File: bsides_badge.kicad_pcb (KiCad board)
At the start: 2 copper layers, 100.5 x 100.5 mm, 2 parts

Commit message: V2 badge
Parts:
- removed the REF** at (125.0, 60.0)
- removed the REF** at (175.0, 60.0)
- added BT1: Battery_Cell, badge:CoinCell_no_silk, F.Cu at (99.7, 83.8)
- added D1: LED, LEDs:LED_0805, F.Cu at (165.7, 53.3)
- added G***: LOGO, graphics:bsides, F.Cu at (135.6, 68.5)
- added J1: Conn_01x16, Pin_Headers:Pin_Header_Straight_1x16_Pitch2.54mm, F.Cu at (106.7, 55.9)
- added J2: Conn_01x01, Pin_Headers:Pin_Header_Straight_1x01_Pitch2.54mm, F.Cu at (111.8, 55.9)
- added R1: 56R, Resistors_SMD:R_0805_HandSoldering, F.Cu at (153.0, 53.3)
- added REF**: keychain_hole, badge:keychain_hole, F.Cu at (96.5, 73.7)
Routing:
- net Net-(J1-Pad1): track 0.00 -> 120.4 mm
- net Net-(BT1-Pad2): track 0.00 -> 81.6 mm
- net Net-(BT1-Pad1): track 0.00 -> 79.5 mm
- net Net-(D1-Pad2): track 0.00 -> 10.2 mm
- added copper zone on F.Cu, net (none)
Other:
- board size 100.5 x 100.5 mm -> 88.9 x 50.8 mm
- net class Default: clearance 0.2 -> 0.4; trace_width 0.25 -> 0.5
- rule trace_clearance: 0.2 -> 0.4

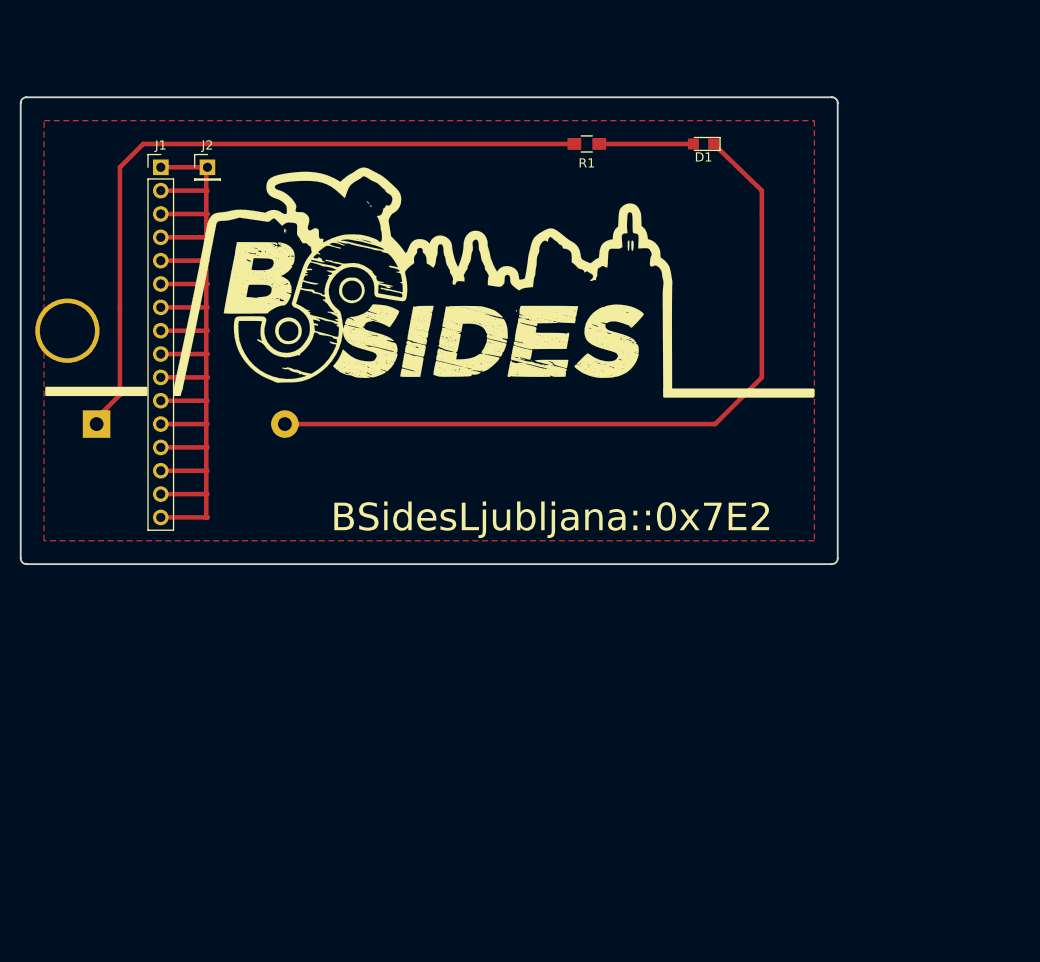
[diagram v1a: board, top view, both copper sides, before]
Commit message: Change to credit card format and rebalanced battery
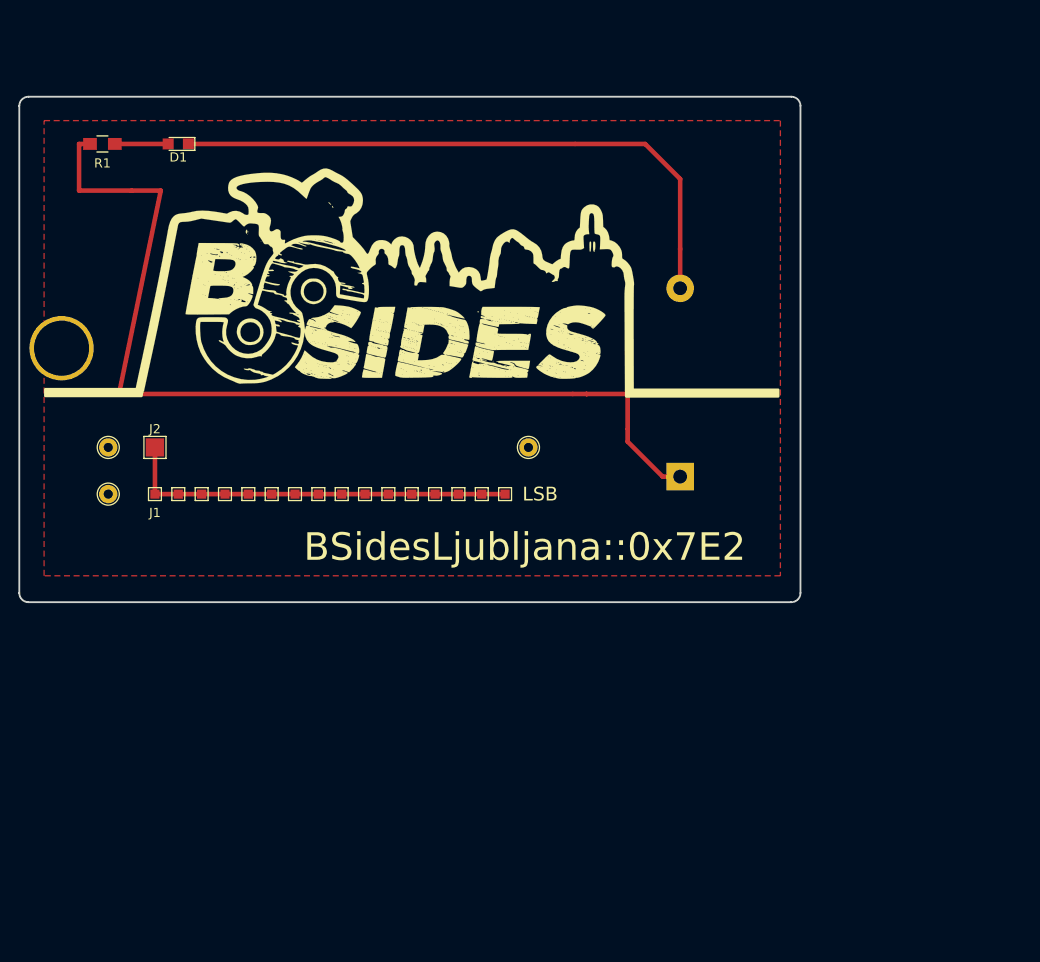
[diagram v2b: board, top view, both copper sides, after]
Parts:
- removed the J1 at (106.7, 55.9)
- added J1: Conn_01x16, TestPoint:TestPoint_Pad_1.0x1.0mm, F.Cu at (144.1, 91.4)
- added J1: Conn_01x16, TestPoint:TestPoint_Pad_1.0x1.0mm, F.Cu at (121.3, 91.4)
- added J1: Conn_01x16, TestPoint:TestPoint_Pad_1.0x1.0mm, F.Cu at (118.7, 91.4)
- added J1: Conn_01x16, TestPoint:TestPoint_Pad_1.0x1.0mm, F.Cu at (116.2, 91.4)
- added J1: Conn_01x16, TestPoint:TestPoint_Pad_1.0x1.0mm, F.Cu at (113.7, 91.4)
- added J1: Conn_01x16, TestPoint:TestPoint_Pad_1.0x1.0mm, F.Cu at (111.1, 91.4)
- added J1: Conn_01x16, TestPoint:TestPoint_Pad_1.0x1.0mm, F.Cu at (108.6, 91.4)
- added J1: Conn_01x16, TestPoint:TestPoint_Pad_1.0x1.0mm, F.Cu at (106.0, 91.4)
- added J1: Conn_01x16, TestPoint:TestPoint_Pad_1.0x1.0mm, F.Cu at (141.6, 91.4)
- added J1: Conn_01x16, TestPoint:TestPoint_Pad_1.0x1.0mm, F.Cu at (139.1, 91.4)
- added J1: Conn_01x16, TestPoint:TestPoint_Pad_1.0x1.0mm, F.Cu at (136.5, 91.4)
- added J1: Conn_01x16, TestPoint:TestPoint_Pad_1.0x1.0mm, F.Cu at (134.0, 91.4)
- added J1: Conn_01x16, TestPoint:TestPoint_Pad_1.0x1.0mm, F.Cu at (131.4, 91.4)
- added J1: Conn_01x16, TestPoint:TestPoint_Pad_1.0x1.0mm, F.Cu at (128.9, 91.4)
- added J1: Conn_01x16, TestPoint:TestPoint_Pad_1.0x1.0mm, F.Cu at (126.4, 91.4)
- added J1: Conn_01x16, TestPoint:TestPoint_Pad_1.0x1.0mm, F.Cu at (123.8, 91.4)
- added REF**: TestPoint_THTPad_D2.0mm_Drill1.0mm, TestPoint:TestPoint_THTPad_D2.0mm_Drill1.0mm, F.Cu at (101.0, 91.4)
- added REF**: TestPoint_THTPad_D2.0mm_Drill1.0mm, TestPoint:TestPoint_THTPad_D2.0mm_Drill1.0mm, F.Cu at (101.0, 86.4)
- added REF**: TestPoint_THTPad_D2.0mm_Drill1.0mm, TestPoint:TestPoint_THTPad_D2.0mm_Drill1.0mm, F.Cu at (146.7, 86.4)
- J2: footprint Pin_Headers:Pin_Header_Straight_1x01_Pitch2.54mm -> TestPoint:TestPoint_Pad_2.0x2.0mm
- moved BT1 63.8 mm to (163.2, 89.5), turned to 90 degrees
- moved D1 57.2 mm to (108.6, 53.3)
- moved R1 52.7 mm to (100.3, 53.3)
- moved J2 31.0 mm to (106.0, 86.4)
- moved G*** 4.17 mm to (131.4, 68.6)
- moved REF** 2.01 mm to (95.9, 75.6)
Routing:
- net Net-(J1-Pad1): track 120.4 -> 43.2 mm
- net Net-(BT1-Pad1): track 79.5 -> 105.6 mm
- net Net-(BT1-Pad2): track 81.6 -> 67.0 mm
- net Net-(D1-Pad2): track 10.2 -> 5.80 mm
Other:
- board size 88.9 x 50.8 mm -> 85 x 55 mm
- board text added: "LSB"
